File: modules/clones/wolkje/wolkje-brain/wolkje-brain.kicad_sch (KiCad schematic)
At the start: 3 parts, among them J4 AUDIO_IN_OUT, J5 LED_DRIVER, J7 Power

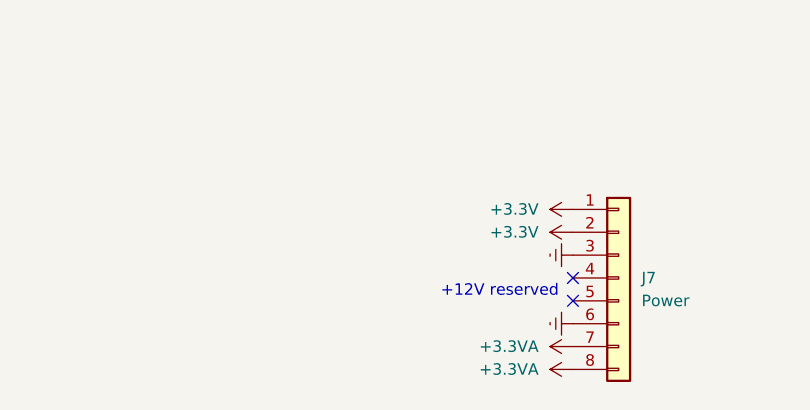
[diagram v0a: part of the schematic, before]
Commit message: debugging and rework for ricochet, midas, wolkje. Added IBOM for drums and other modules.
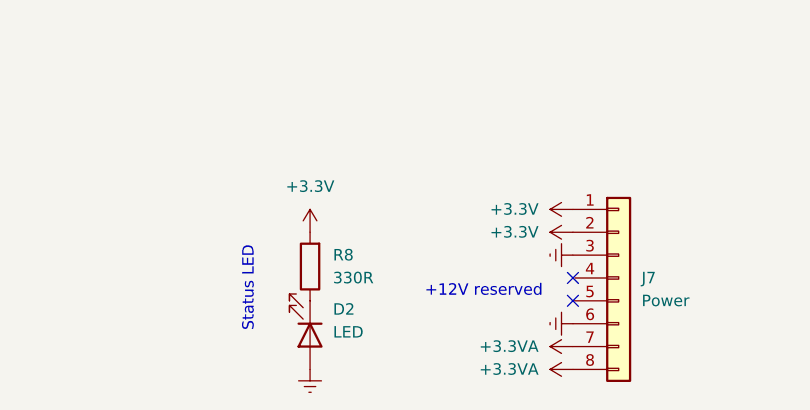
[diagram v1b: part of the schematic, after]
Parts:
- added D2: LED, LED_SMD:LED_0805_2012Metric_Pad1.15x1.40mm_HandSolder, symbol Device:LED
- added R8: 330R, Resistor_SMD:R_0805_2012Metric_Pad1.20x1.40mm_HandSolder, symbol Device:R
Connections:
- net +3.3V: now also R8.2
- net GNDREF: now also D2.2 (A)
- new net: D2.1 (K), R8.1
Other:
- note added: "Status LED"

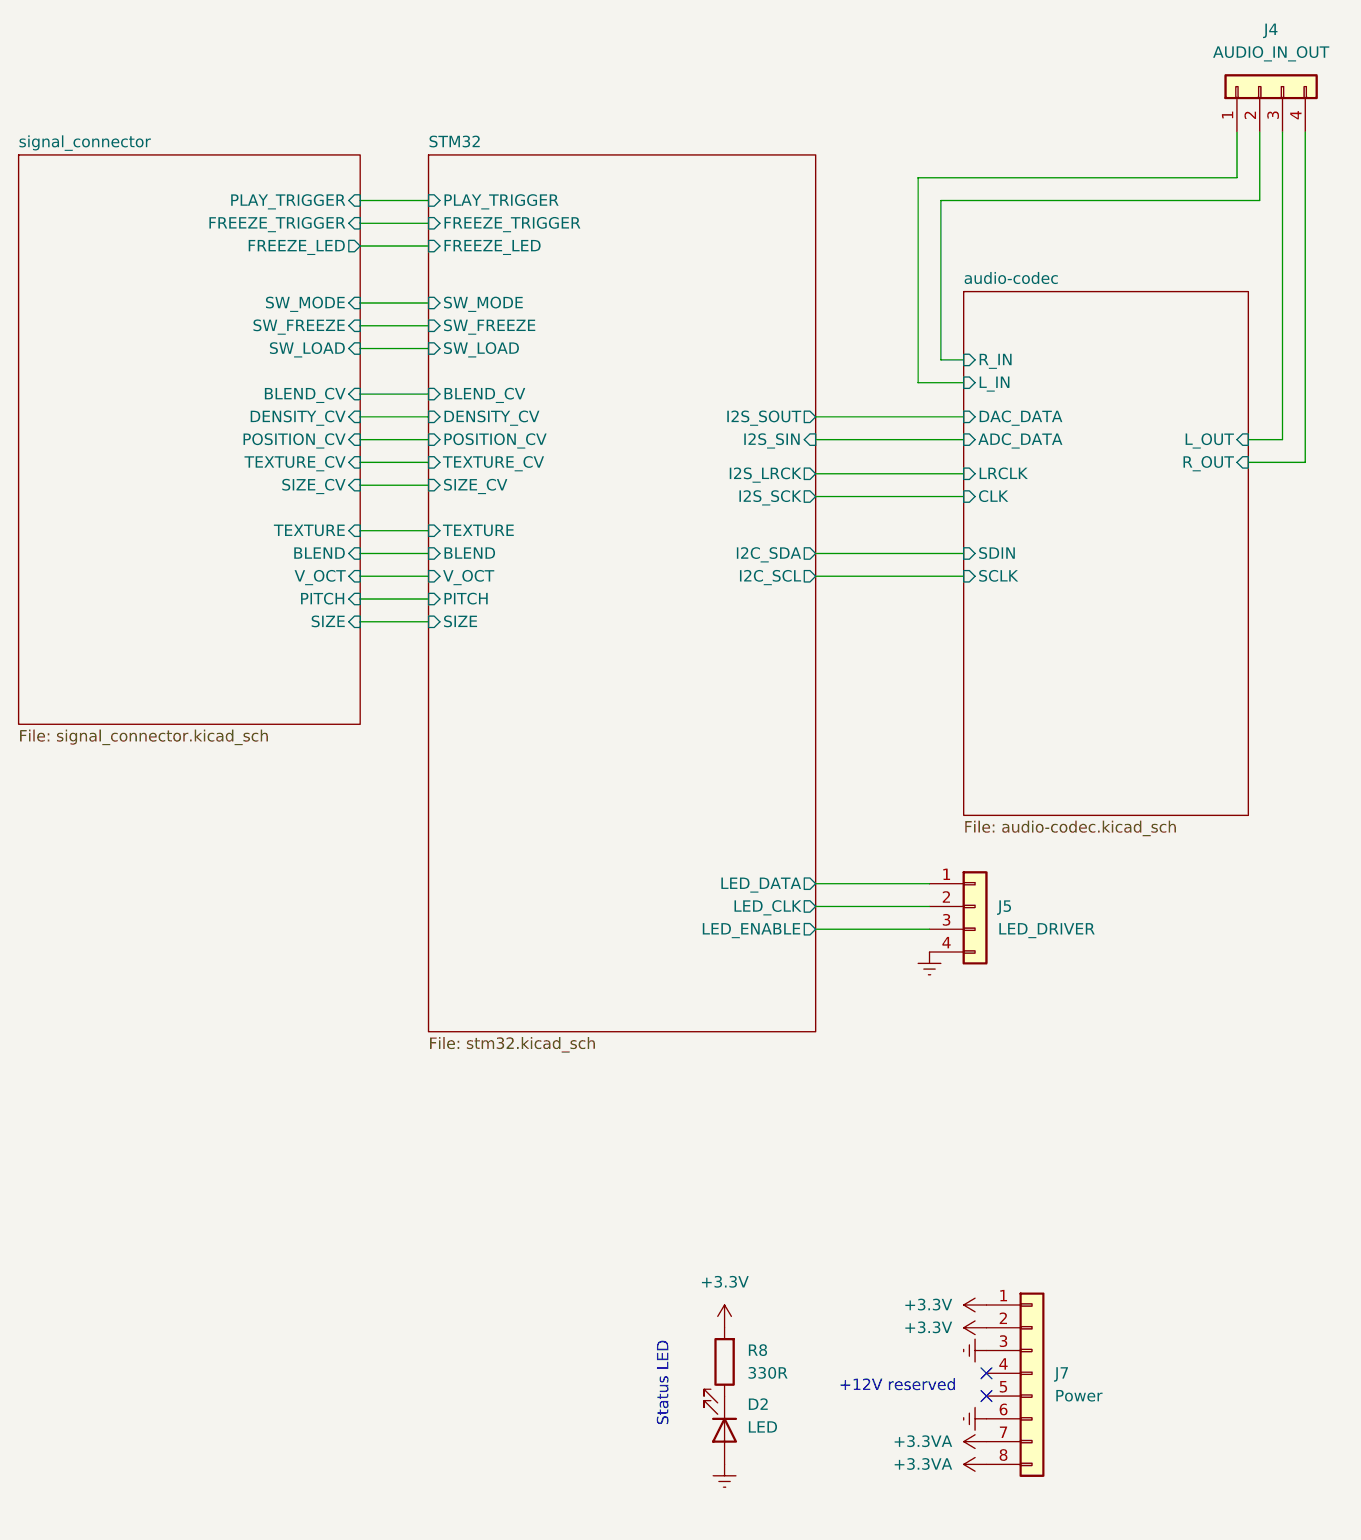
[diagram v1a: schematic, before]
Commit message: Preperation for Run3, wolkje, ricochet readme and final exports
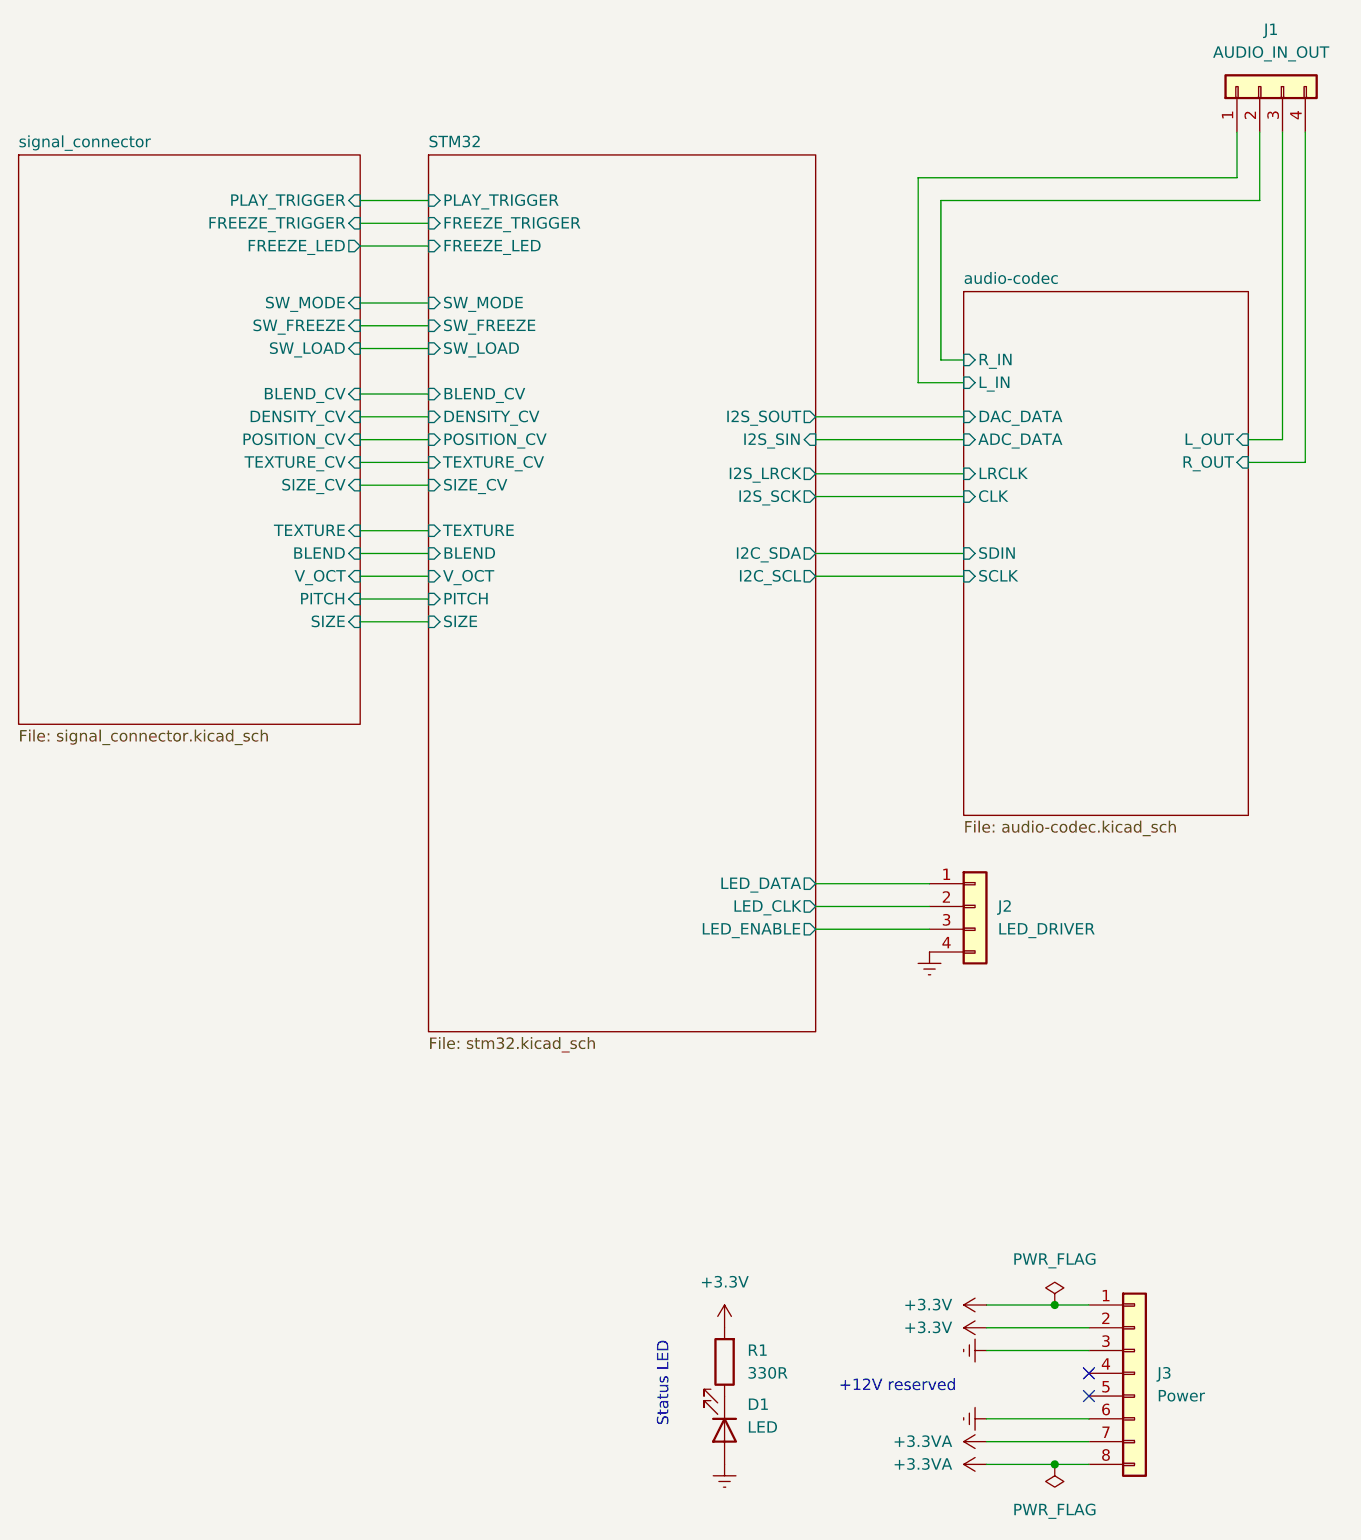
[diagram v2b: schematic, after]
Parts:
- renumbered D2 to D1, J4 to J1, J5 to J2, J7 to J3, R8 to R1
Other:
- moved on the sheet: J3

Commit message: finished clouds clone (weathering/the storm)
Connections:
- net GNDREF: now also D1.1 (K); no longer D1.2 (A)
- net at R1.1: now also D1.2 (A); no longer D1.1 (K)
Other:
- moved on the sheet: D1
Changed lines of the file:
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@@
 	(symbol
 		(lib_id "Device:LED")
-		(at 125.73 184.15 270)
+		(at 125.73 184.15 90)
 		(unit 1)
 		(exclude_from_sim no)
@@
 		(fields_autoplaced yes)
 		(property "Reference" "D1"
-			(at 128.27 181.2924 90)
+			(at 129.54 184.4674 90)
 			(effects
 				(font
 					(size 1.27 1.27)
 				)
-				(justify left)
+				(justify right)
 			)
 		)
 		(property "Value" "LED"
-			(at 128.27 183.8324 90)
+			(at 129.54 187.0074 90)
 			(effects
 				(font
 					(size 1.27 1.27)
 				)
-				(justify left)
+				(justify right)
 			)
 		)
